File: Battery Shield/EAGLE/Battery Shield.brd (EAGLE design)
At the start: 22.8 x 39 mm, 30 parts, among them IC1 MCP73871, U1 TPS61200

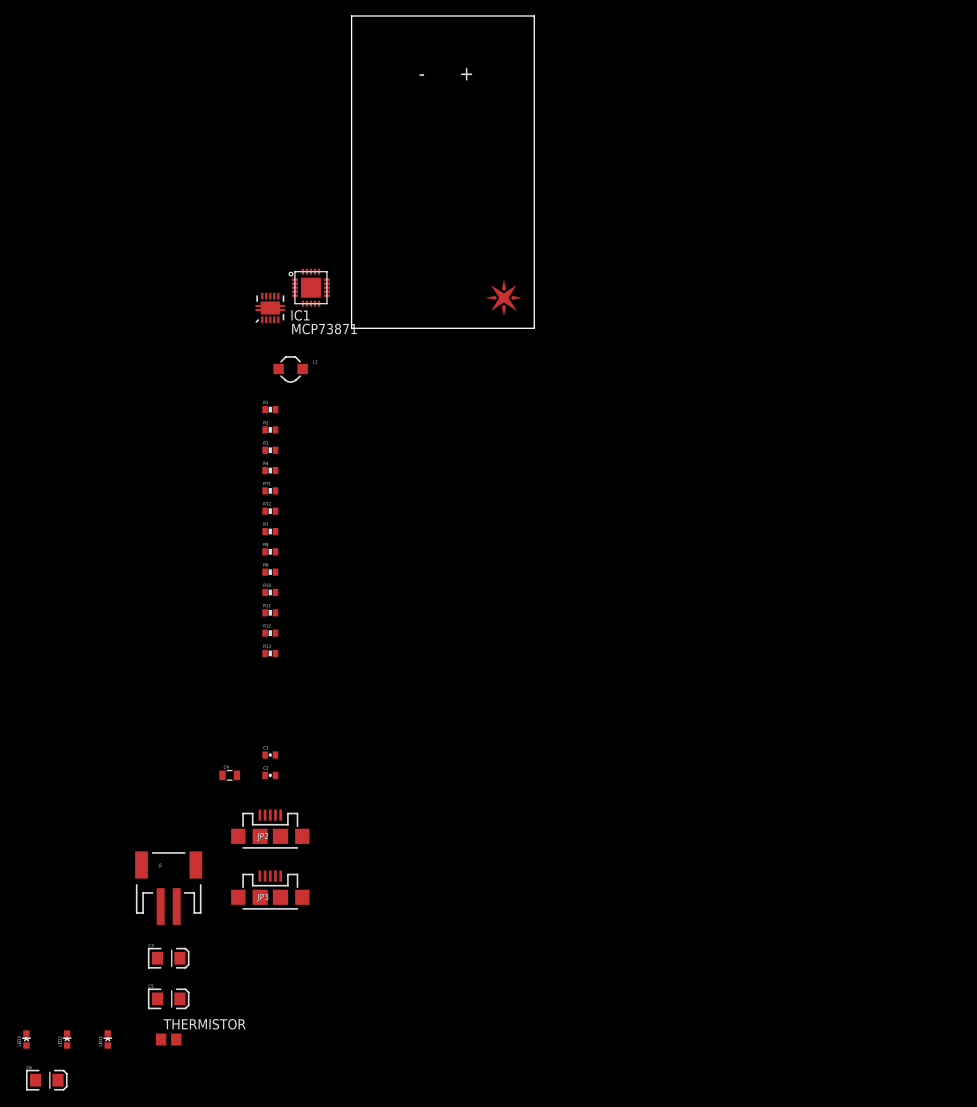
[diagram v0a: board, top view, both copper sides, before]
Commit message: updated the battery shield and created the BOM
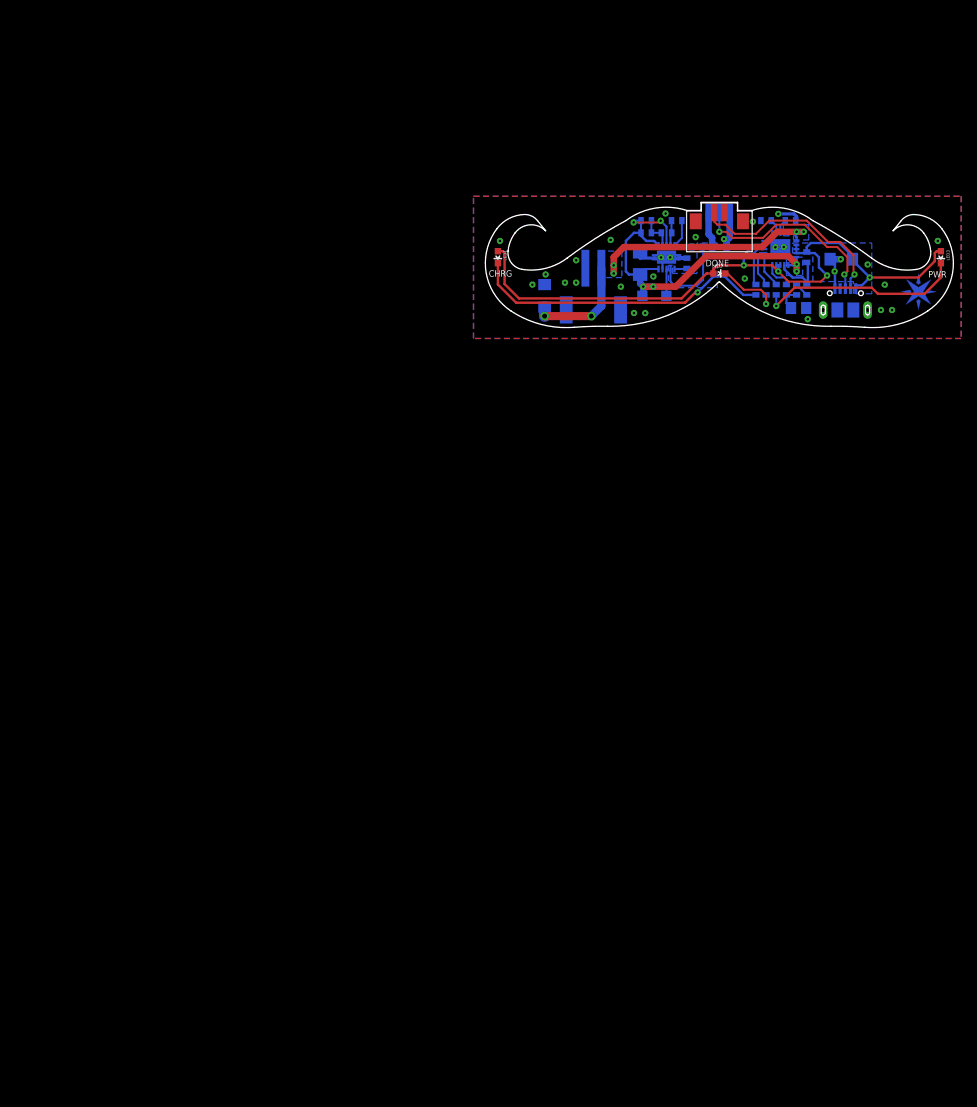
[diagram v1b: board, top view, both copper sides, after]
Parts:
- removed JP2, JP3: USB-MICROB, SparkFun-Connectors:USB-MICROB
- added JP1: USBUSB-MICROB-SLOT-HOLE, Spark:USB-MICROB-SLOT-HOLE
- added U$1: USB_MALE, Spark:USB-MICROB-MALE-SANDWICH
- C5: device SparkFun-Capacitors:EIA3216 -> SparkFun-Capacitors:1206
- L1: value (none) -> 4.7uH, 1.2A
- LED1: value (none) -> Yellow
- LED2: value (none) -> Green
- LED3: value (none) -> Red
- R1, R3: value (none) -> 2M
- R11, R12, R13: value (none) -> 1K
- R2, R4: value (none) -> 220K
- moved LED3 150.4 mm to (73.7, 8.89), turned to 180 degrees
- moved C6 142.8 mm to (61.2, 8.64), flipped to the bottom, turned to 180 degrees
- moved LED2 125.8 mm to (46.0, 6.86), turned to 270 degrees
- moved THERMISTOR 120.7 mm to (55.9, 2.54), flipped to the bottom, turned to 180 degrees
- moved LED1 109.3 mm to (18.3, 8.89), turned to 180 degrees
- moved C5 109.2 mm to (36.1, 8.13), flipped to the bottom, turned to 90 degrees
- moved C3 95.2 mm to (24.1, 4.06), flipped to the bottom, turned to 270 degrees
- moved C4 90.1 mm to (46.0, 10.3), flipped to the bottom, turned to 180 degrees
- moved J1 89.8 mm to (30.2, 3.81), flipped to the bottom, turned to 180 degrees
- moved C2 82.5 mm to (36.8, 11.9), flipped to the bottom, turned to 180 degrees
- moved C1 80.6 mm to (41.9, 8.13), flipped to the bottom, turned to 90 degrees
- moved R13 77.9 mm to (53.1, 4.83), flipped to the bottom, turned to 270 degrees
- moved R9 77.8 mm to (56.9, 8.89), flipped to the bottom, turned to 90 degrees
- moved R8 77.1 mm to (54.9, 13.5), flipped to the bottom
- moved R10 77.0 mm to (56.9, 4.83), flipped to the bottom, turned to 90 degrees
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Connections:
- removed net N$17: IC1.8, LED1.C
- new net N$16: LED3.C, R13.2
- net +5V: now also U$1.VBUS; no longer JP3.VBUS
- net D+: now also JP1.D+, U$1.D+; no longer JP2.D+, JP3.D+
- net D-: now also JP1.D-, U$1.D-; no longer JP2.D-, JP3.D-
- net GND: now also C5.2, JP1.GND, JP1.MT1, JP1.MT2, U$1.GND, U$1.GNDPAD1, U$1.GNDPAD2; no longer C5.C, JP2.GND, JP2.MT1, JP2.MT2, JP3.GND, JP3.MT1, JP3.MT2
- net N$10: now also LED2.C, R12.2; no longer LED3.A, R13.1
- net N$14: now also R12.1; no longer LED2.C
- net N$15: now also R13.1; no longer LED3.C
- net N$6: now also IC1.8; no longer LED1.A
- net N$8: now also LED1.C, R11.2; no longer LED2.A, R12.1
- net VBATT_OUT: now also C5.1, U1.6, U1.8; no longer C5.A
- net VBUS: now also JP1.VBUS, LED1.A, LED2.A, LED3.A; no longer JP2.VBUS, R11.2, R12.2, R13.2
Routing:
- net VBUS: track 0.00 -> 87.5 mm, vias 0 -> 4
- net VBATT_OUT: track 0.00 -> 51.6 mm, vias 0 -> 5
- net N$5: track 0.00 -> 42.8 mm, vias 0 -> 6
- net N$8: track 0.00 -> 38.2 mm, vias 0 -> 1
- net GND: track 0.00 -> 29.3 mm, vias 0 -> 29
- net D-: track 0.00 -> 26.1 mm, vias 0 -> 1
- net N$16: track 0.00 -> 25.9 mm, vias 0 -> 1
- net D+: track 0.00 -> 25.2 mm, vias 0 -> 2
- net +5V: track 0.00 -> 16.0 mm
- net N$10: track 0.00 -> 8.46 mm, vias 0 -> 1
- net N$12: track 0.00 -> 7.30 mm
- net N$4: track 0.00 -> 5.72 mm
- net N$6: track 0.00 -> 5.54 mm
- net N$14: track 0.00 -> 4.99 mm
- net N$3: track 0.00 -> 4.40 mm
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- added copper zone on layer 16, net +5V
- added copper zone on layer 1, net GND
- added copper zone on layer 16, net GND
- added copper zone on layer 16, net N$5
- added copper zone on layer 16, net VBATT_OUT
- added copper zone on layer 16, net VBUS
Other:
- board size 22.8 x 39 mm -> 58.5 x 15.7 mm
- board text added: "Battery Shield"
- board text added: "CHRG"
- board text added: "DONE"
- board text added: "PWR"
- board text removed: "+"
- board text removed: "-"
- board text removed: "Spark Battery Shield v0.1 2013-04-05"
